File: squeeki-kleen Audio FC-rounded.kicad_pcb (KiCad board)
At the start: 2 copper layers, 50.8 x 17.8 mm, 21 parts, among them J1 GND, J2 VCC, J3 P1, J4 P2, J5 C8, J6 GND out, U1 OPA1671IDCKT

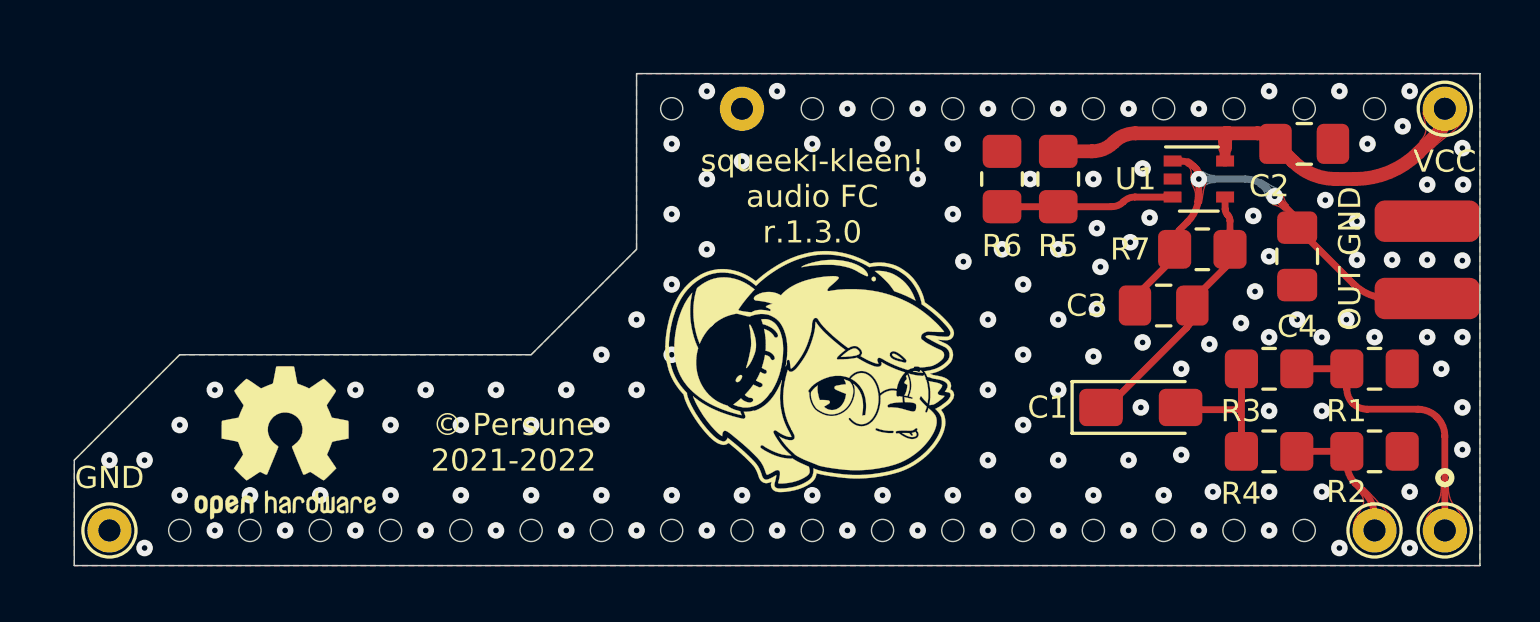
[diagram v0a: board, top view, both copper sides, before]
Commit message: Update board layout, add level adjustment
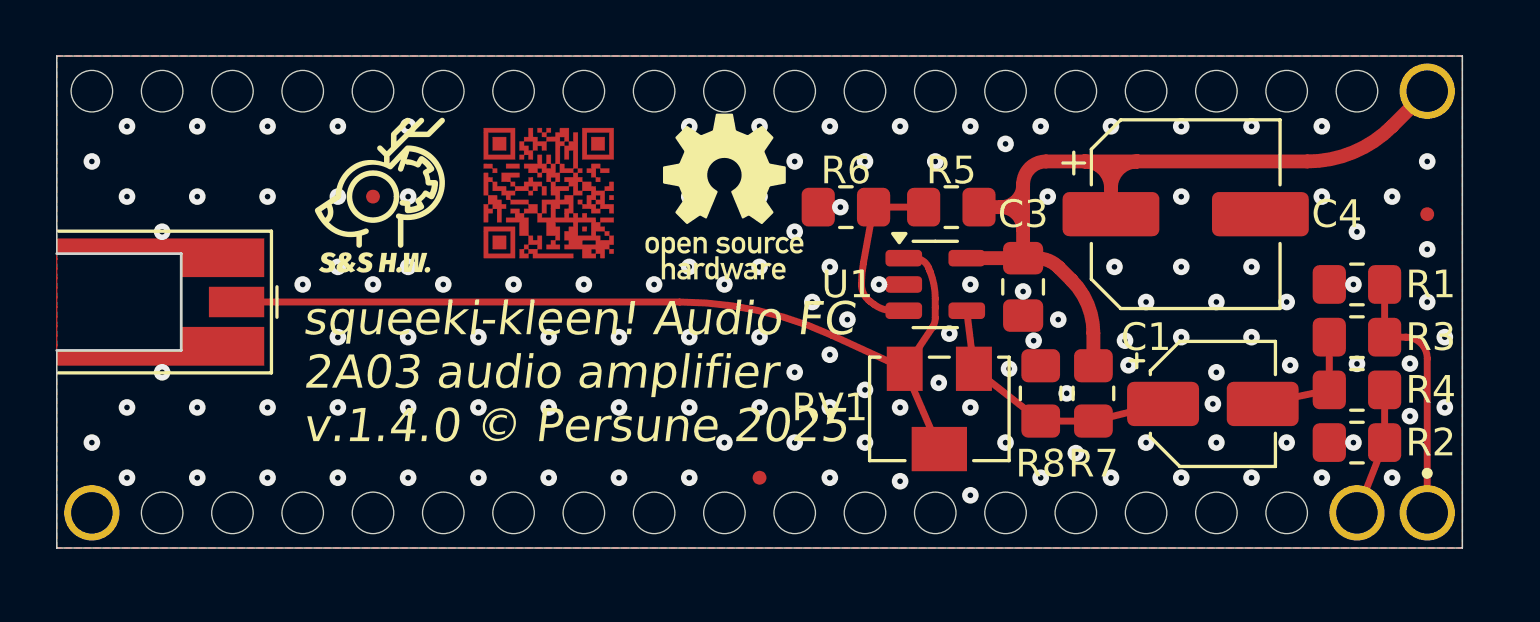
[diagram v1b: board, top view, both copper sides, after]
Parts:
- removed C2: 0.1µF, Capacitor_SMD:C_0805_2012Metric_Pad1.18x1.45mm_HandSolder
- removed G***: LOGO, custom footprints:dagga
- removed J6: GND out, custom footprints:Custom_Pad
- removed the REF** at (48.3, 40.0)
- removed the REF** at (64.8, 27.9)
- added ?: , , F.Cu at (48.9, 42.5)
- added ?: , , F.Cu at (56.5, 27.3)
- added ?: , , F.Cu at (41.3, 27.3)
- added ?: , , F.Cu at (43.8, 42.5)
- added ?: , , F.Cu at (56.5, 42.5)
- added ?: , , F.Cu at (59.1, 27.3)
- added ?: , , F.Cu at (51.4, 27.3)
- added ?: , , F.Cu at (69.2, 42.5)
- added ?: , , F.Cu at (79.4, 42.5)
- added ?: , , F.Cu at (61.6, 42.5)
- added ?: , , F.Cu at (51.4, 42.5)
- added ?: , , F.Cu at (54.0, 42.5)
- added ?: , , F.Cu at (66.7, 42.5)
- added ?: , , F.Cu at (69.2, 27.3)
- added ?: , , F.Cu at (81.9, 27.3)
- added ?: , , F.Cu at (43.8, 27.3)
- added ?: , , F.Cu at (59.1, 42.5)
- added ?: , , F.Cu at (71.8, 42.5)
- added ?: , , F.Cu at (66.7, 27.3)
- added ?: , , F.Cu at (84.5, 42.5)
- added ?: , , F.Cu at (81.9, 42.5)
- added ?: , , F.Cu at (48.9, 27.3)
- added ?: , , F.Cu at (76.8, 42.5)
- added ?: , , F.Cu at (79.4, 27.3)
- added ?: , , F.Cu at (87.0, 27.3)
- added ?: , , F.Cu at (64.1, 27.3)
- added ?: , , F.Cu at (64.1, 42.5)
- added ?: , , F.Cu at (74.3, 42.5)
- added ?: , , F.Cu at (84.5, 27.3)
- added ?: , , F.Cu at (46.4, 27.3)
- added ?: , , F.Cu at (54.0, 27.3)
- added ?: , , F.Cu at (76.8, 27.3)
- added ?: , , F.Cu at (46.4, 42.5)
- added ?: , , F.Cu at (71.8, 27.3)
- added ?: , , F.Cu at (74.3, 27.3)
- added ?: , , F.Cu at (61.6, 27.3)
- added R8: 68K, Resistor_SMD:R_0805_2012Metric_Pad1.20x1.40mm_HandSolder, F.Cu at (75.6, 38.2)
- added REF**: Fiducial_0.5mm_Mask1.5mm, Fiducial:Fiducial_0.5mm_Mask1.5mm, F.Cu at (65.4, 41.3)
- added REF**: Fiducial_0.5mm_Mask1.5mm, Fiducial:Fiducial_0.5mm_Mask1.5mm, F.Cu at (89.5, 31.8)
- added REF**: Fiducial_0.5mm_Mask1.5mm, Fiducial:Fiducial_0.5mm_Mask1.5mm, F.Cu at (51.4, 31.1)
- added RV1: 100K, Potentiometer_SMD:Potentiometer_Bourns_3224W_Vertical, F.Cu at (71.9, 38.8)
- added Ref**: Val**, custom footprints:qr, F.Cu at (57.8, 31.0)
- added svg2mod: G***, custom footprints:oshw-logo 6x6mm, F.Cu at (64.1, 31.1)
- added svg2mod: G***, custom footprints:maustech icon fiducial 0-50mm 1-50mm, F.Cu at (51.4, 31.1)
- C1: footprint Capacitor_Tantalum_SMD:CP_EIA-3216-18_Kemet-A_Pad1.58x1.35mm_HandSolder -> Capacitor_SMD:CP_Elec_4x5.4
- C3: value 82pF -> 0.1µF
- C4: value 0.1µF -> 100µF; footprint Capacitor_SMD:C_0805_2012Metric_Pad1.18x1.45mm_HandSolder -> Capacitor_SMD:CP_Elec_6.3x4.5
- J5: value C8 -> Conn_Coaxial; footprint custom footprints:Custom_Pad -> Connector_Coaxial:MMCX_Molex_73415-0961_Horizontal_0.8mm-PCB
- R5: value 10K -> 47K
- R6: value 10K -> 68K
- R7: value 80K -> 47K
- U1: value OPA1671IDCKT -> TL971; footprint Package_TO_SOT_SMD:SOT-353_SC-70-5 -> Package_TO_SOT_SMD:SOT-23-5
- moved J5 45.8 mm to (43.8, 34.9), turned to 0 degrees
- moved U1 10.3 mm to (71.8, 34.3)
- moved R7 6.53 mm to (77.5, 38.2), turned to -90 degrees
- moved R6 5.73 mm to (68.5, 31.5), turned to 180 degrees
- moved C3 5.12 mm to (74.9, 34.4), turned to -90 degrees
- moved C4 4.31 mm to (80.8, 31.8), turned to 0 degrees
- moved R5 4.00 mm to (72.3, 31.5), turned to 180 degrees
- moved R4 3.88 mm to (87.0, 38.1)
- moved R3 3.37 mm to (87.0, 36.2)
- moved R1 3.11 mm to (87.0, 34.3), turned to 0 degrees
- moved C1 2.61 mm to (81.8, 38.6)
- moved J2 0.90 mm to (89.5, 27.3)
- moved J3 0.90 mm to (89.5, 42.5), turned to 0 degrees
- moved J1 0.90 mm to (41.3, 42.5), turned to 0 degrees
- moved J4 0.90 mm to (87.0, 42.5), turned to 0 degrees
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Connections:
- C1 pad 1: Net-(C1-Pad1) -> Net-(U1--)
- C3 pad 1: Net-(C1-Pad1) -> VCC
- C3 pad 2: /C8 -> GND
- C4 pad 1: /C8 -> VCC
- R7 pad 1: Net-(C1-Pad1) -> VCC
- R7 pad 2: /C8 -> Net-(U1--)
- U1 pad 4: Net-(C1-Pad1) -> Net-(U1--)
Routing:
- net VCC: track 17.2 -> 34.0 mm
- net /C8: track 16.7 -> 32.8 mm, vias 2 -> 0
- net Net-(U1--): track 0.00 -> 9.68 mm
- net Net-(C1-Pad1): track 9.63 -> 0.00 mm
- net Net-(U1-+): track 6.25 -> 7.33 mm
- net /P1: track 10.4 -> 9.43 mm
- net Net-(C1-Pad2): track 5.18 -> 4.37 mm
- net GND: vias 134 -> 132
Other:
- outline, holes or cut-outs redrawn
- board text added: "squeeki-kleen! Audio FC 2A03 audio amplifier v.1.4.0 © Persune 2025"
- board text removed: "GND"
- board text removed: "OUT"
- board text removed: "squeeki-kleen! audio FC r.1.3.0"
- board text removed: "© Persune 2021-2022"
